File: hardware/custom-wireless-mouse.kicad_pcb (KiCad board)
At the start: 2 copper layers, 48 x 64 mm, 34 parts, among them J1 SWD_HEADER, J2 B2B-XH-A, Q1 DMG2305UXQ, SW1 JS202011SCQN, SW2 D2FC-F-7N(20M), SW3 D2FC-F-7N(20M), SW4 D2FC-F-7N(20M), SW5 B3U-1000P, U1 nRF52810-QCAA-T, U2 PMW3610DM-SUDU, U3 TLV61220DBVT, Y1 NX2016SA-32MHZ

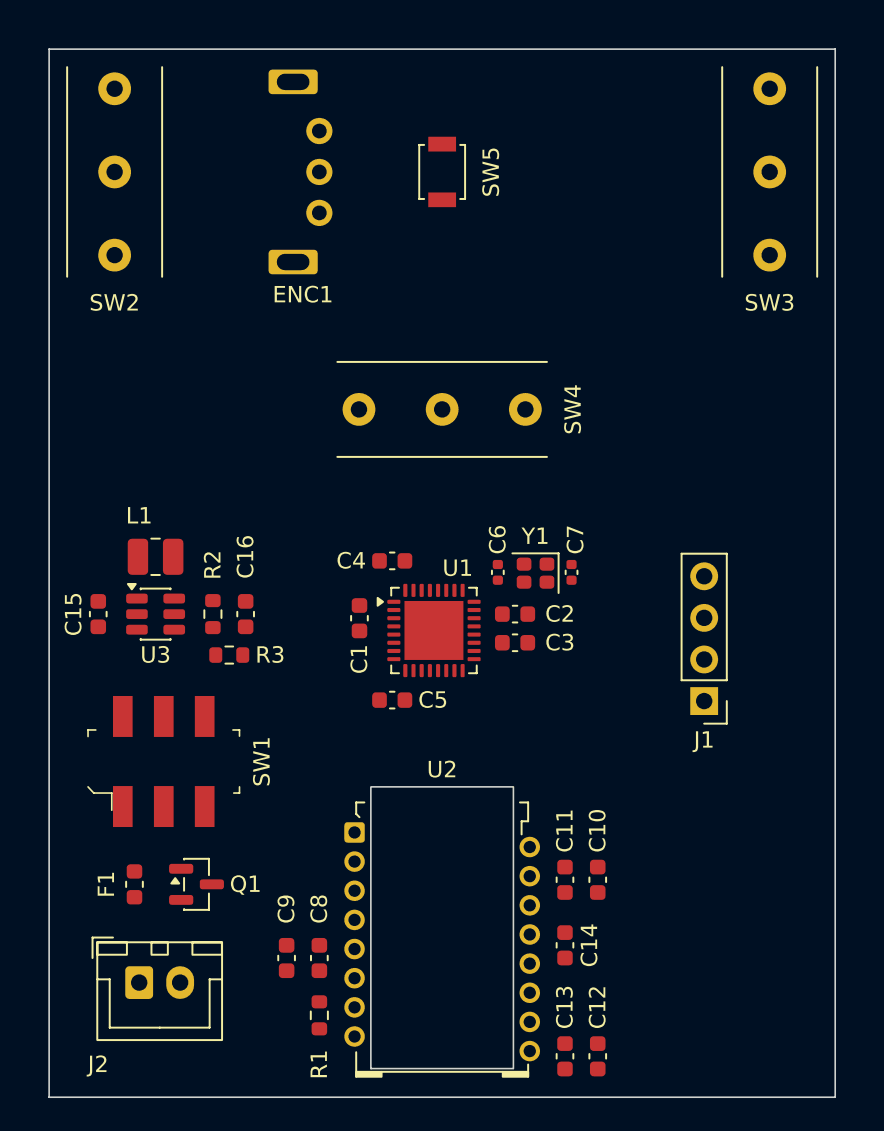
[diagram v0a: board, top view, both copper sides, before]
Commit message: First-pass routing, remove function button, rewire SW5
Routed the board (ENC1/SW2/SW3/SW5/U1/U3/J1/J2/Q1/antenna feed all
connected) and placed a meandered PCB trace antenna. DRC dropped from
13 violations / 53 unconnected items to 1 violation / 0 unconnected.

Removed SW4 (function/DPI button) for lack of routing space -- dropped
its footprint, its BTN_FN net, and the now-stale references across
docs. U1 pin 15 (P0.20) is now a spare no-connect GPIO. Any DPI/secondary
function will need to be remapped onto the remaining buttons in firmware.

Rewired SW5 (pin 1 -> BTN_SCRL, pin 2 -> GND, matching the old D2FC's
mapping) and placed it on the PCB next to ENC1.

Logged the one remaining DRC error in open-items.md: the antenna feed
trace clips the board's own "Antenna" keepout zone, which currently
disallows tracks/vias there as well as copper pour -- needs a layout
decision, not a doc fix.

Co-Authored-By: Claude Sonnet 5 <noreply@anthropic.com>
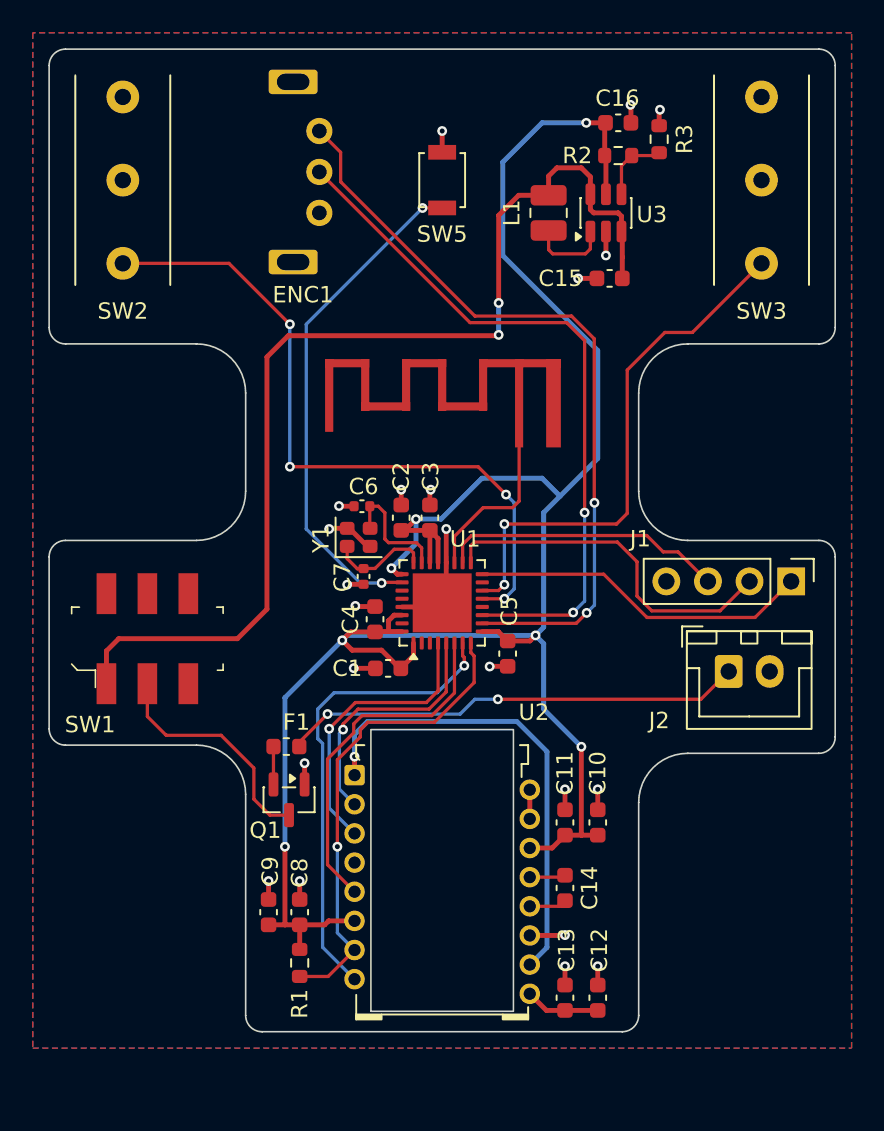
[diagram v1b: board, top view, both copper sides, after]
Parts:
- removed SW4: D2FC-F-7N(20M), omron-d2fc-f-7n:switch-tht-omron-d2fc-f-7n
- moved R3 41.0 mm to (37.2, 11.5), turned to 90 degrees
- moved J2 40.7 mm to (41.5, 44.0)
- moved C16 37.7 mm to (34.8, 10.5), turned to 0 degrees
- moved R2 37.4 mm to (34.8, 12.5), turned to 0 degrees
- moved C15 37.4 mm to (34.2, 20.0), turned to 180 degrees
- moved U3 36.8 mm to (34.0, 16.0), turned to 90 degrees
- moved L1 31.9 mm to (30.5, 16.0), turned to -90 degrees
- moved C7 12.7 mm to (19.2, 38.2)
- moved F1 12.5 mm to (14.5, 48.6), turned to 180 degrees
- moved Y1 11.0 mm to (18.9, 35.8), turned to 0 degrees
- moved C3 9.24 mm to (23.2, 34.6), turned to 90 degrees
- moved C6 9.23 mm to (19.1, 33.9), turned to 0 degrees
- moved C2 9.11 mm to (21.5, 34.6), turned to 90 degrees
- moved J1 9.04 mm to (45.3, 38.5), turned to -90 degrees
- moved Q1 7.65 mm to (14.7, 51.8), turned to -90 degrees
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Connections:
- U1 pad 15: /BTN_FN -> unconnected-(U1-P0.20-Pad15)
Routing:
- net +VSYS: track 0.00 -> 137.1 mm, vias 0 -> 7
- net /VBAT_SW: track 0.00 -> 65.9 mm, vias 0 -> 2
- net /WHEEL_A: track 0.00 -> 46.7 mm, vias 0 -> 2
- net /WHEEL_B: track 0.00 -> 43.0 mm, vias 0 -> 2
- net /BTN_L: track 0.00 -> 42.5 mm, vias 0 -> 4
- net GND: track 0.00 -> 34.1 mm, vias 0 -> 22
- net /BTN_R: track 0.00 -> 32.6 mm, vias 0 -> 2
- net /BTN_SCRL: track 0.00 -> 31.0 mm, vias 0 -> 2
- net /SENS_NRESET: track 0.00 -> 29.4 mm, vias 0 -> 1
- net /SENS_MOTION: track 0.00 -> 28.9 mm, vias 0 -> 1
- net Net-(U2-+VCSEL): track 0.00 -> 28.8 mm, vias 0 -> 1
- net Net-(J2-+): track 0.00 -> 28.3 mm, vias 0 -> 2
- net /SWDCLK: track 0.00 -> 21.9 mm
- net /SPI_NCS: track 0.00 -> 21.6 mm
- net /nRESET: track 0.00 -> 20.9 mm
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- added copper zone on B.Cu, net GND
- added copper zone on F.Cu, net GND
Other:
- board size 48 x 64 mm -> 48 x 60 mm

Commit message: Resize vias to meet JLCPCB's annular ring minimum
All 50 vias were reworked and resized to 0.8mm pad / 0.3mm drill
(0.25mm annular ring), meeting JLCPCB's recommended value rather than
just their 0.18mm absolute minimum for a 2-layer board. DRC confirms no
new violations (still only the pre-existing antenna-keepout error, 0
unconnected items).

Updated the project's net-class via defaults and min_via_annular_width
DRC rule to match, so future vias added via the GUI default to a
JLCPCB-compliant size. Docs updated to mark this resolved.

Co-Authored-By: Claude Sonnet 5 <noreply@anthropic.com>
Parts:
- moved F1 0.19 mm to (14.5, 48.4)
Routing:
- net /BTN_L: track 42.5 -> 43.4 mm
- net GND: track 34.1 -> 34.8 mm
- net /SENS_MOTION: track 28.9 -> 29.6 mm
- net /SPI_SCLK: track 17.6 -> 18.1 mm
- net /WHEEL_A: track 46.7 -> 47.2 mm
